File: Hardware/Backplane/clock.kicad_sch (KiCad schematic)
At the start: 6 parts, among them U201 OSC48M-3.3I/S3-20T, U202 SN74LVC7001A

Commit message: Some cleanups of Backplane schematic: Adds DigiKey part numbers, removes unnecessary properties, marks test points as excluded from BOM
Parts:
- U201: Digikey Part No (none) -> 3155-OSC48M-3.3I/S3-20TCT-ND
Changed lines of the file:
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@@
 			)
 		)
-		(property "Datasheet" "~"
+		(property "Datasheet" ""
 			(at 28.575 41.275 0)
 			(effects
@@
 			)
 		)
-		(property "Datasheet" "~"
+		(property "Datasheet" ""
 			(at 34.925 41.275 0)
 			(effects
@@
 			(at 64.77 40.005 0)
 			(effects
+				(font
+					(size 1.27 1.27)
+				)
+				(hide yes)
+			)
+		)
+		(property "Digikey Part No" "3155-OSC48M-3.3I/S3-20TCT-ND"
+			(at 64.77 40.005 0)
+			(effects

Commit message: Adjusts to review comments
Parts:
- added R203: 10K, Resistor_SMD:R_0603_1608Metric, symbol Device:R
- C204: Digikey Part No (none) -> 399-C0603C104M4RACTUCT-ND
- C205: Digikey Part No (none) -> 399-C0603C103K5RACTUCT-ND
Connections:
- net +3V3: now also R203.2; no longer U202.1 (1A), U202.12 (4A), U202.4 (2A), U202.9 (3A)
- new net: R203.1, U202.1 (1A), U202.12 (4A), U202.4 (2A), U202.9 (3A)
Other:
- moved on the sheet: U202

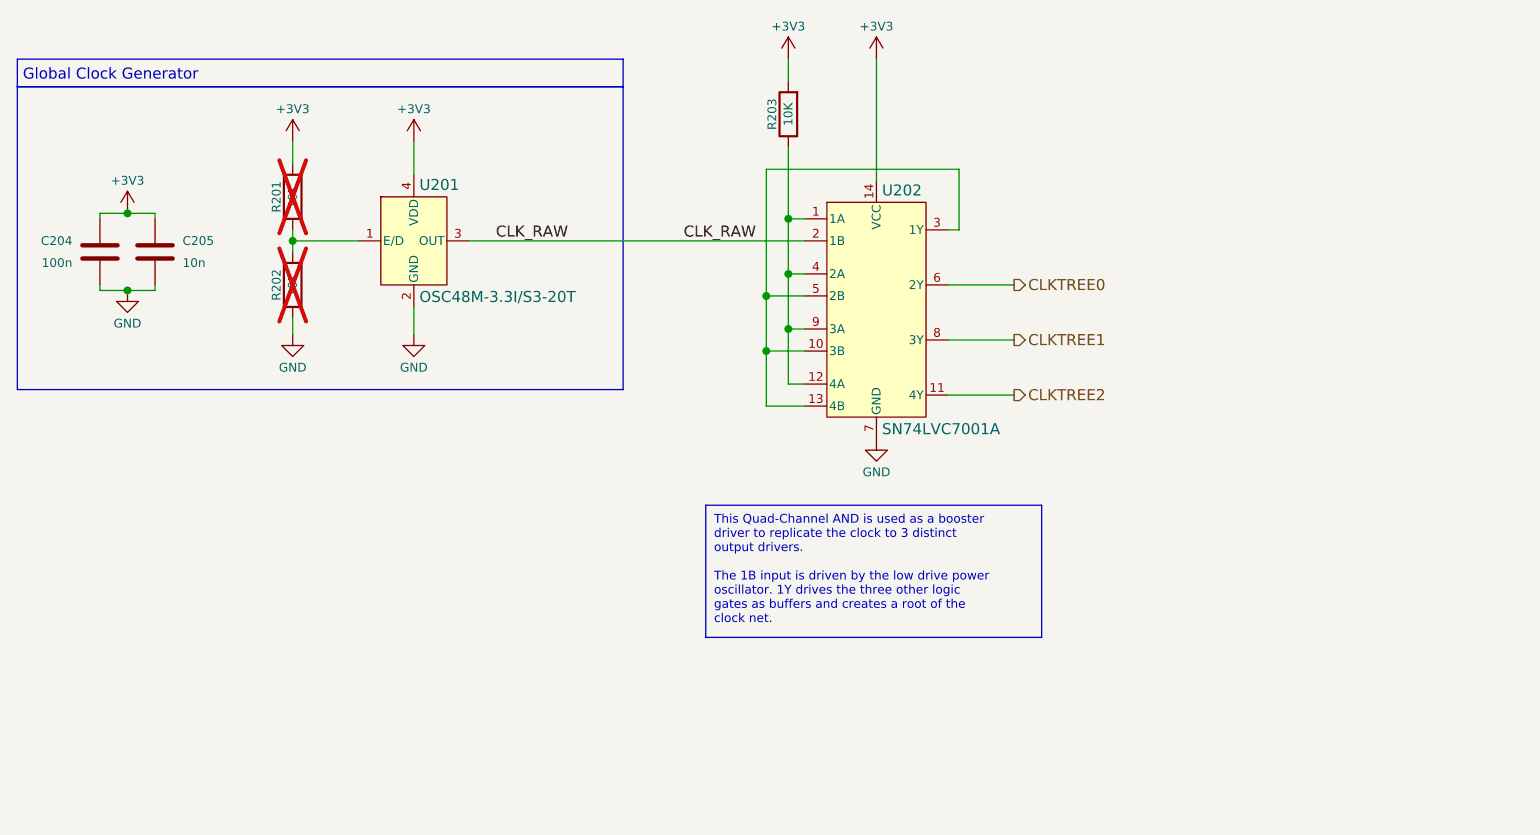
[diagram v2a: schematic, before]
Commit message: Starts refactoring Backplane to use NL17SZS11-D instead of 4-port AND
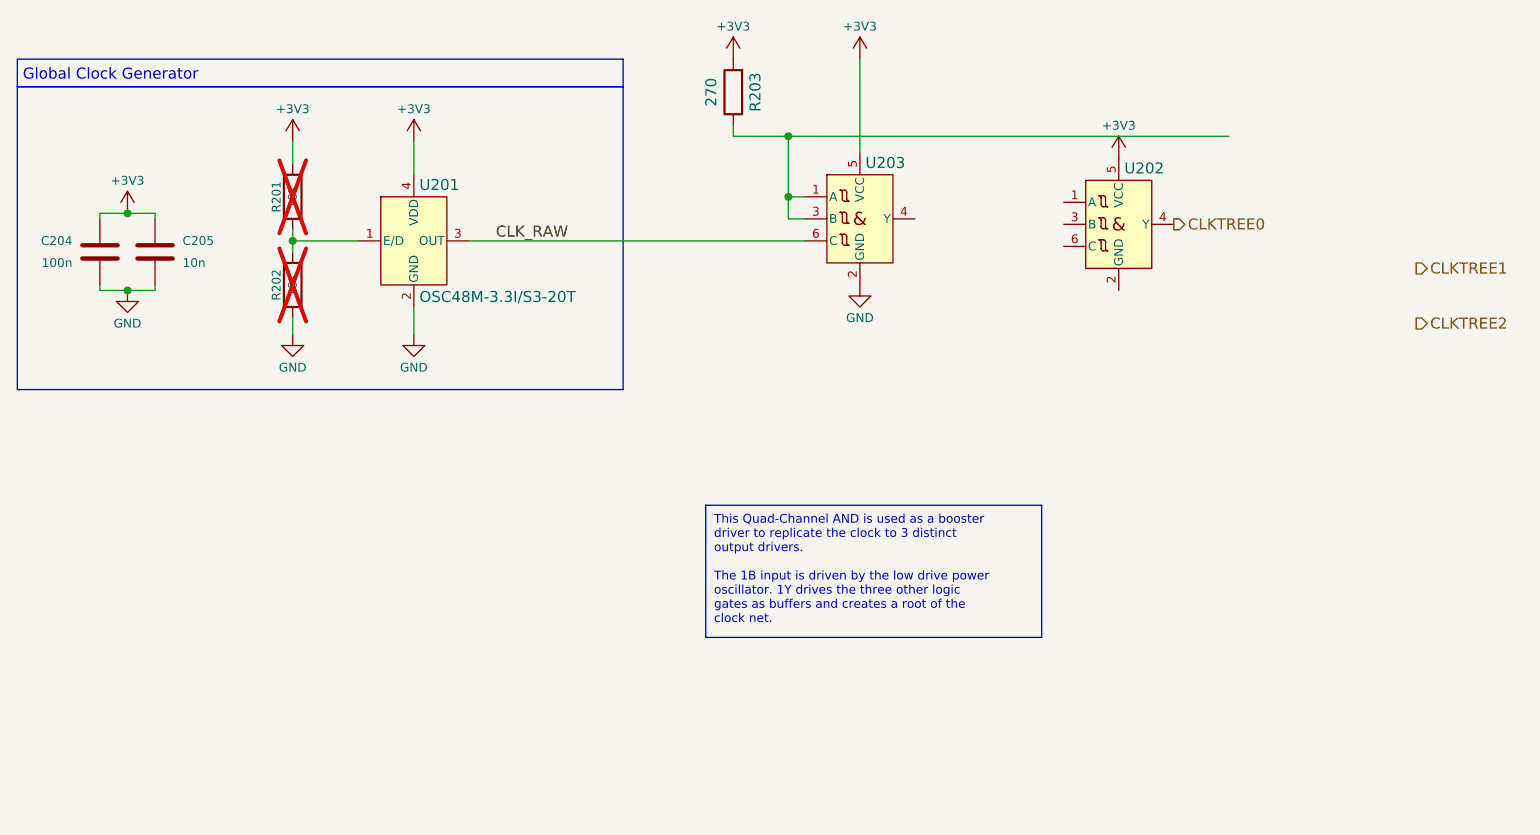
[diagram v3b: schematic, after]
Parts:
- removed U202: SN74LVC7001A, symbol Home Computer:SN74LVC7001APWR
- added U202, U203: NL17SZS11DFT2G-Q, Package_TO_SOT_SMD:SOT-363_SC-70-6, symbol Home Computer:NL17SZS11DFT2G-Q
- R203: value 10K -> 270; Digikey Part No 311-10.0KHRCT-ND -> RMCF0603FT270RCT-ND
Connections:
- net +3V3: now also U202.5 (VCC), U203.5 (VCC)
- net CLKTREE0: now also U202.4 (Y)
- net CLK_RAW: now also U203.6 (C)
- net GND: now also U203.2 (GND)
- net at R203.1: now also U203.1 (A), U203.3 (B)

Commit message: Cleans up Backplane schematic even more. Less parts in the BOM, less mistakes!
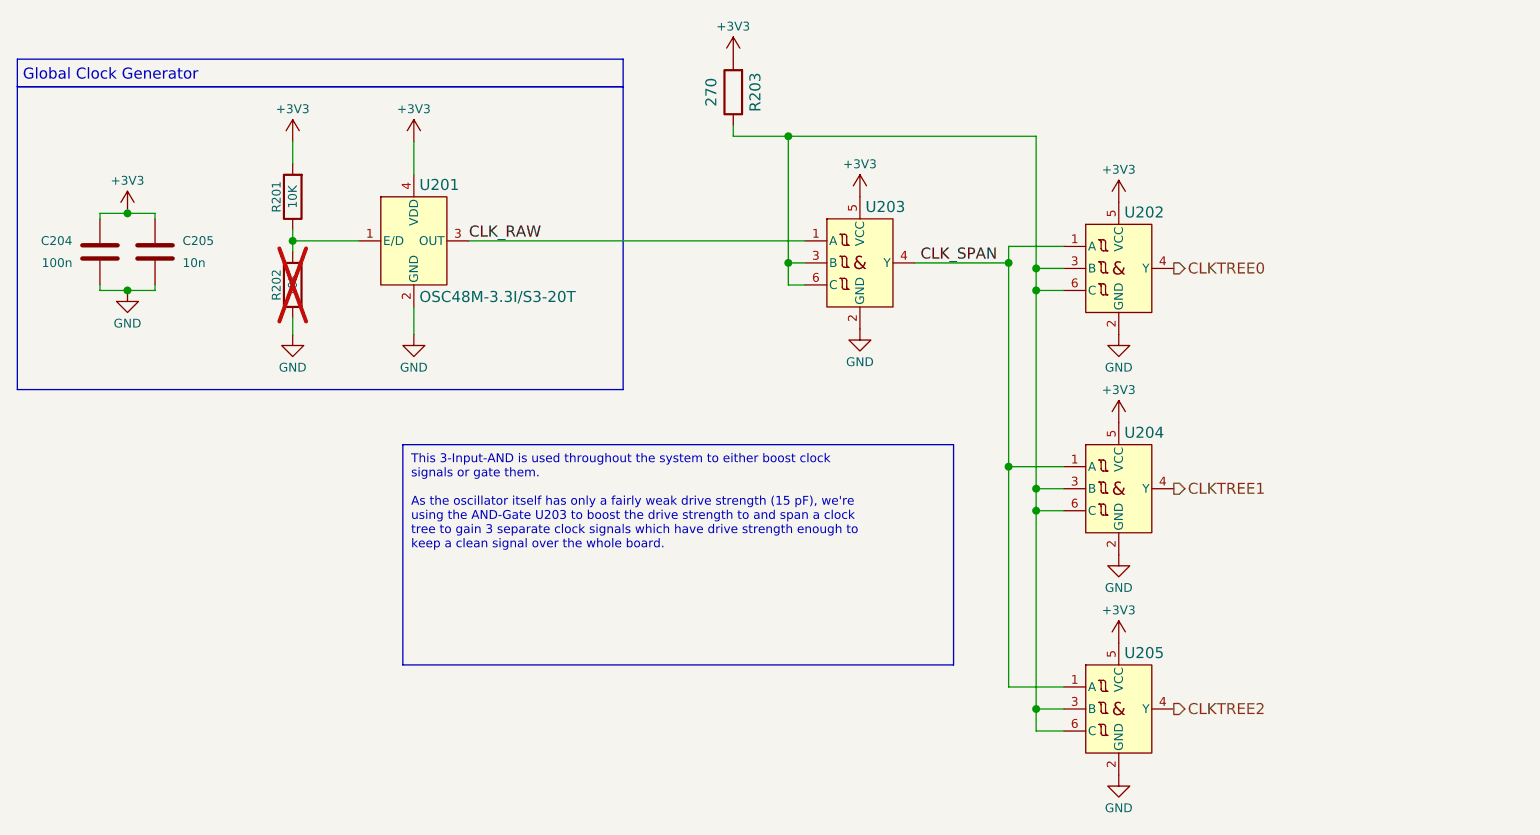
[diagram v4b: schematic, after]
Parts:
- added U204, U205: NL17SZS11DFT2G-Q, Package_TO_SOT_SMD:SOT-363_SC-70-6, symbol Home Computer:NL17SZS11DFT2G-Q
- R201: now fitted
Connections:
- net +3V3: now also U204.5 (VCC), U205.5 (VCC)
- net CLKTREE1: now also U204.4 (Y)
- net CLKTREE2: now also U205.4 (Y)
- net CLK_RAW: now also U203.1 (A); no longer U203.6 (C)
- net GND: now also U202.2 (GND), U204.2 (GND), U205.2 (GND)
- net CLK_SPAN: now reaches U202.1 (A)
- net CLK_SPAN: now also U203.4 (Y), U204.1 (A), U205.1 (A)
- net at U202.3 (B): now also R203.1, U202.6 (C), U203.3 (B), U203.6 (C), U204.3 (B), U204.6 (C), U205.3 (B), U205.6 (C)
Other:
- moved on the sheet: U202, U203

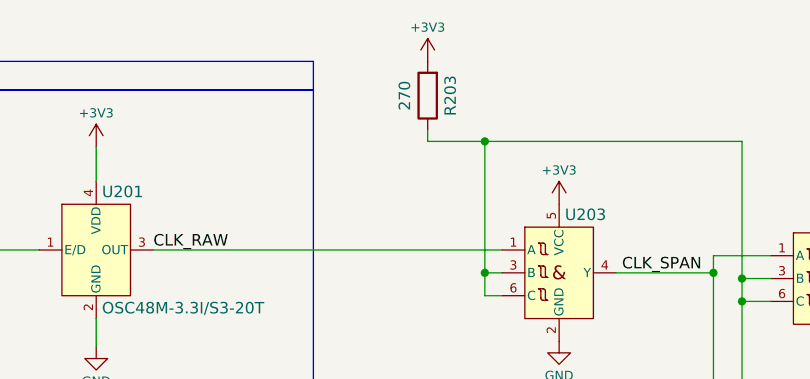
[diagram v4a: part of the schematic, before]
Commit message: Cleans up schematic even more, consolidates 270 and 100 Ohm resistors into the 560 ohm resistor, as they were only used as series resistors for the mosfets and LED current limiters
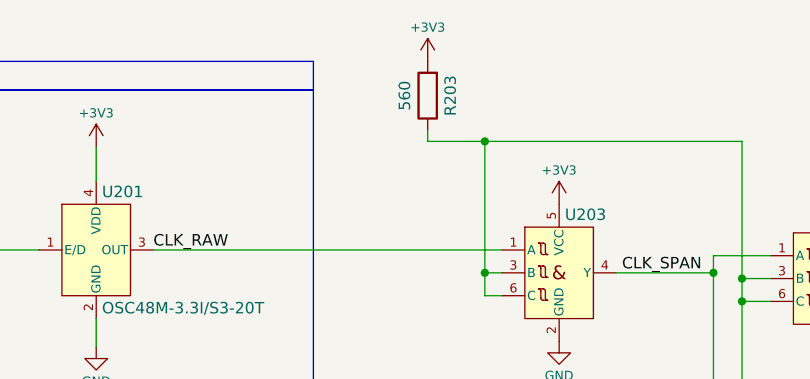
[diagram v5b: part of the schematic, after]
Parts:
- R203: value 270 -> 560; Digikey Part No RMCF0603FT270RCT-ND -> RR08P560DCT-ND
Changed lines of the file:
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@@
 			)
 		)
-		(property "Value" "270"
+		(property "Value" "560"
 			(at 99.06 22.86 90)
 			(effects
@@
 			)
 		)
-		(property "Datasheet" "https://www.seielect.com/catalog/SEI-RMCF_RMCP.pdf"
+		(property "Datasheet" "https://www.susumu.co.jp/common/pdf/n_catalog_partition05_en.pdf"
 			(at 101.6 22.86 0)
 			(effects
@@
 			)
 		)
-		(property "Digikey Part No" "RMCF0603FT270RCT-ND"
+		(property "Digikey Part No" "RR08P560DCT-ND"
 			(at 101.6 22.86 90)
 			(effects

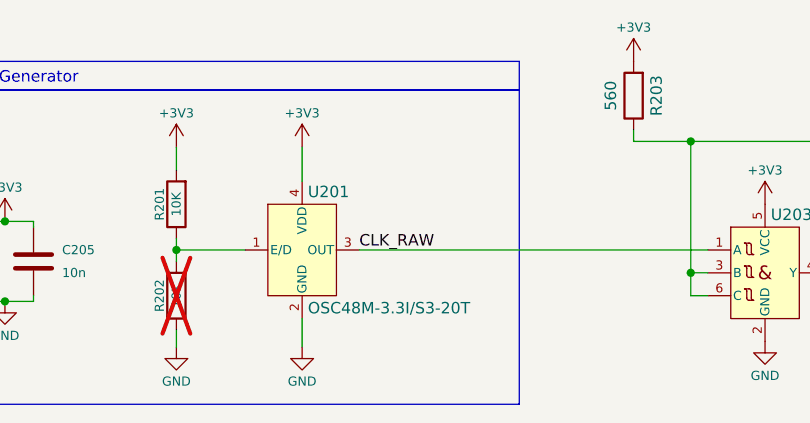
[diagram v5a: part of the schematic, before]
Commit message: More BOM consolidation
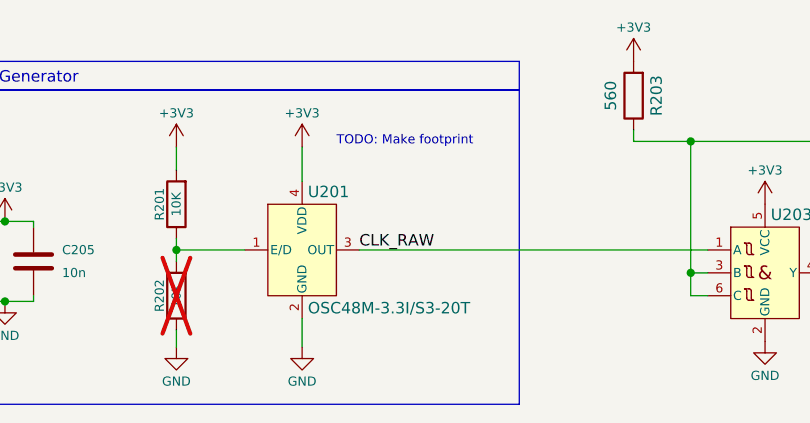
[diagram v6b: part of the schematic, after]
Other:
- note added: "TODO: Make footprint"
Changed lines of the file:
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@@
+		)
+	)
+	(text "TODO: Make footprint"
+		(exclude_from_sim no)
+		(at 76.2 27.94 0)
+		(effects
+			(font
+				(size 1.016 1.016)
+			)
 		)
 	)

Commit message: Upgrades schematic files to KiCAD 10.0
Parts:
- U202, U203, U204, U205: DigiKey Part No 488-NL17SZS11DFT2G-QCT-ND -> (none); Digikey Part No (none) -> 488-NL17SZS11DFT2G-QCT-ND

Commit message: Further backplane PCB cleanup.
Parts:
- U201: footprint (none) -> Crystal:Crystal_SMD_Abracon_ABM8AIG-4Pin_3.2x2.5mm
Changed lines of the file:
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@@
 			)
 		)
-		(property "Footprint" ""
+		(property "Footprint" "Crystal:Crystal_SMD_Abracon_ABM8AIG-4Pin_3.2x2.5mm"
 			(at 64.77 40.005 0)
 			(hide yes)
@@
 			)
 		)
-		(property "Description" ""
+		(property "Description" "48 MHz XO (Standard) CMOS Oscillator 3.3V Enable/Disable 4-SMD, No Lead"
 			(at 64.77 40.005 0)
 			(hide yes)
